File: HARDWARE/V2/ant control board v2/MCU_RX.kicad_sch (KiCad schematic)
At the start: 22 parts, among them J10 ELRS, SW1 BOOT, U10 FS2A 4CH reciever, U11 AT24C02C, U9 STM32F072CBTx

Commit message: layout 2.0 facv2 done
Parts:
- removed C14: 100n, Capacitor_SMD:C_0603_1608Metric, symbol Device:C
- removed TP3: SWDIO, TestPoint:TestPoint_Pad_D1.0mm, symbol Connector:TestPoint
- removed TP4: SWCLK, TestPoint:TestPoint_Pad_D1.0mm, symbol Connector:TestPoint
- added Q1: PNM3FD20V1E, Package_DFN_QFN:Diodes_DFN1006-3, symbol Simulation_SPICE:NMOS
- added R10: 5.1k, Resistor_SMD:R_0402_1005Metric, symbol Device:R
- C13: renamed from C15; footprint Capacitor_SMD:C_0603_1608Metric -> Capacitor_SMD:C_0402_1005Metric
- C14: renamed from C16; footprint Capacitor_SMD:C_0603_1608Metric -> Capacitor_SMD:C_0402_1005Metric; LCSC C282519 -> C1525
- C15: renamed from C17; footprint Capacitor_SMD:C_0603_1608Metric -> Capacitor_SMD:C_0402_1005Metric; LCSC C282519 -> C1525
- C16: renamed from C18; footprint Capacitor_SMD:C_0603_1608Metric -> Capacitor_SMD:C_0402_1005Metric; LCSC C282519 -> C1525
- C17: renamed from C19; footprint Capacitor_SMD:C_0603_1608Metric -> Capacitor_SMD:C_0402_1005Metric; LCSC C282519 -> C1525
- C18: renamed from C20; footprint Capacitor_SMD:C_0603_1608Metric -> Capacitor_SMD:C_0402_1005Metric; LCSC C282519 -> C1525
- C19: renamed from C21; footprint Capacitor_SMD:C_0603_1608Metric -> Capacitor_SMD:C_0402_1005Metric; LCSC C282519 -> C1525
- C20: renamed from C?; footprint Capacitor_SMD:C_0603_1608Metric -> Capacitor_SMD:C_0402_1005Metric; now left out of the parts list
- D2: footprint LED_SMD:LED_0805_2012Metric -> LED_SMD:LED_1206_3216Metric; LCSC C84259 -> C779809
- J12: renamed from J10; footprint (none) -> _MY_connectors:Pad 01x04 small; now left out of the parts list
- R11: renamed from R6; value 1.5k -> 220; footprint Resistor_SMD:R_0603_1608Metric -> Resistor_SMD:R_0402_1005Metric; LCSC C23186 -> C112291
- R7: renamed from R5; footprint Resistor_SMD:R_0603_1608Metric -> Resistor_SMD:R_0402_1005Metric; LCSC C23186 -> C25905
- R8: renamed from R7; footprint Resistor_SMD:R_0603_1608Metric -> Resistor_SMD:R_0402_1005Metric; LCSC C23186 -> C25905
- R9: renamed from R8; footprint Resistor_SMD:R_0603_1608Metric -> Resistor_SMD:R_0402_1005Metric; LCSC C23186 -> C25905
- SW1: footprint _MIA footprint:SW-SMD_TS24CA SMD BUTTO 90deg -> Button_Switch_SMD:SW_SPST_B3U-1000P; LCSC C393942 -> C2885149
- U6: renamed from U9; LCSC (none) -> C81720
- U9: renamed from U?; footprint _My_boards:NRF24L01+ SMD -> _My_modules:NRF24L01+ SMD; now left out of the parts list
- renumbered U10 to U7, U11 to U8
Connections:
- net RESET is gone; now on net +3V3: U6.7 (NRST)
- net GND: now also Q1.2 (S); no longer D2.1 (K), SW1.3 (hold), SW1.4 (hold)
- net NRF24L01_CE: no longer U6.29 (PA8)
- net SERVO1: now also U6.18 (PB0); no longer U6.21 (PB10)
- net SERVO2: now also U6.19 (PB1); no longer U6.22 (PB11)
- net SPI2_MISO: no longer U6.27 (PB14)
- net SPI2_MOSI: no longer U6.28 (PB15)
- net SPI2_NSS: no longer U6.25 (PB12)
- net SPI2_SCK: no longer U6.26 (PB13)
- net UART2_RX: now also J12.2 (Pin_2); no longer J12.1 (Pin_1)
- net UART2_TX: now also J12.1 (Pin_1); no longer J12.2 (Pin_2)
- net at R11.1: now also D2.2 (A); no longer U6.3 (PC14)
- net +BATT: now reaches R11.2
- net +BATT: no longer D2.2 (A)
- new net: D2.1 (K), Q1.3 (D)
- new net: Q1.1 (G), R10.2
- new net STATUS_LED: R10.1, U6.3 (PC14)
- no-connect marks 8 -> 15
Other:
- note added: "STATUS LED"
- moved on the sheet: D2, R11

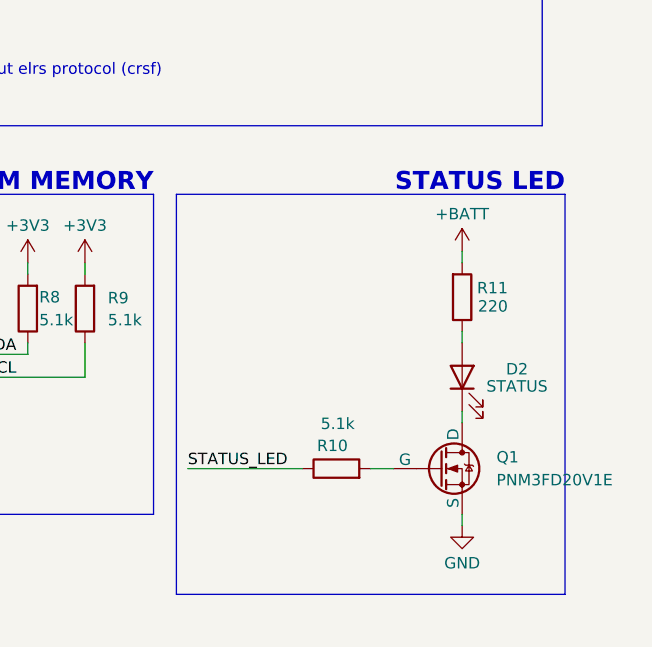
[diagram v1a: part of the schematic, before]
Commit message: adjusted some strace position and teardrops. Fixed silkscreedn
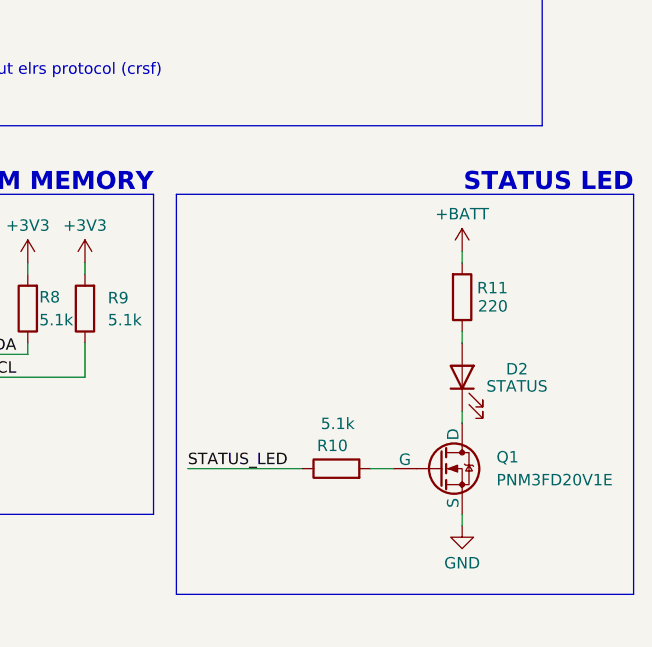
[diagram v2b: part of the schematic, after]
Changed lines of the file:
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@@
 	(rectangle
 		(start 207.01 109.22)
-		(end 250.19 153.67)
+		(end 257.81 153.67)
 		(stroke
 			(width 0)
@@
 	(text "STATUS LED"
 		(exclude_from_sim no)
-		(at 250.19 107.95 0)
+		(at 257.81 107.95 0)
 		(effects
 			(font

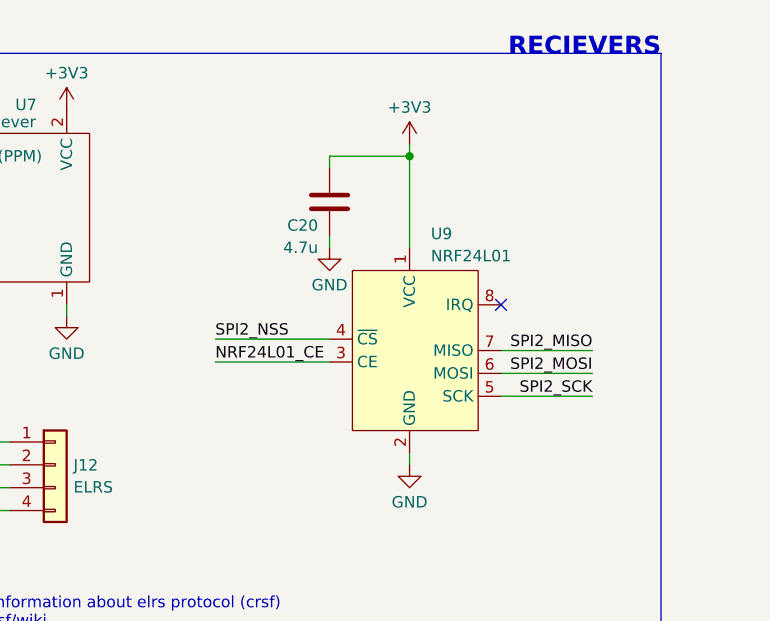
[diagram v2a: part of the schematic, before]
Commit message: Adjusted some pcb things and re generated Prouction files
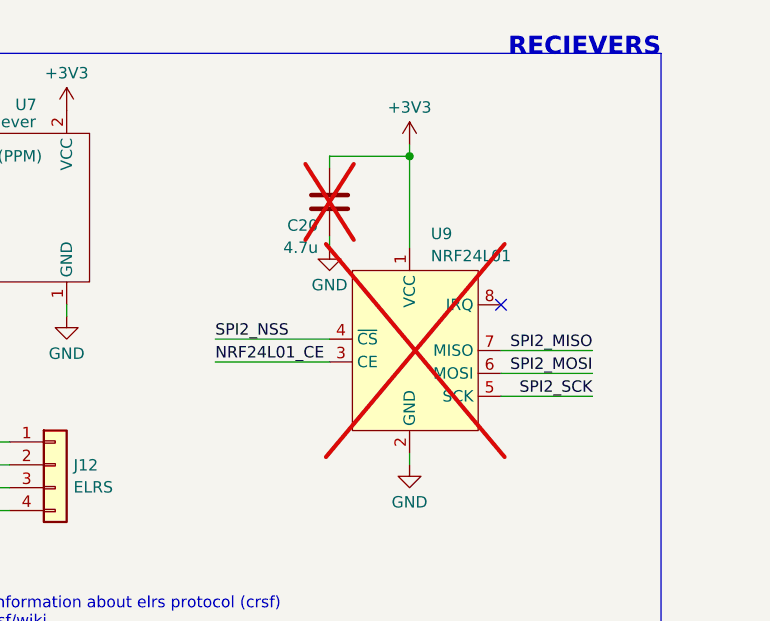
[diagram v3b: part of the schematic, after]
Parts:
- C20, U9: now not fitted
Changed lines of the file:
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@@
 		(in_bom no)
 		(on_board no)
-		(dnp no)
+		(dnp yes)
 		(property "Reference" "C20"
 			(at 209.55 53.4146 0)
@@
 		(in_bom no)
 		(on_board no)
-		(dnp no)
+		(dnp yes)
 		(fields_autoplaced yes)
 		(property "Reference" "U9"
